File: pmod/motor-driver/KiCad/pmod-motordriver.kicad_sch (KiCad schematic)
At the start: 14 parts, among them J1 Conn_01x06_Pin, J2 Screw_Terminal_01x02, J3 Screw_Terminal_01x02, J4 Screw_Terminal_01x02, Q1 AO3401A, U1 DRV8833PWP

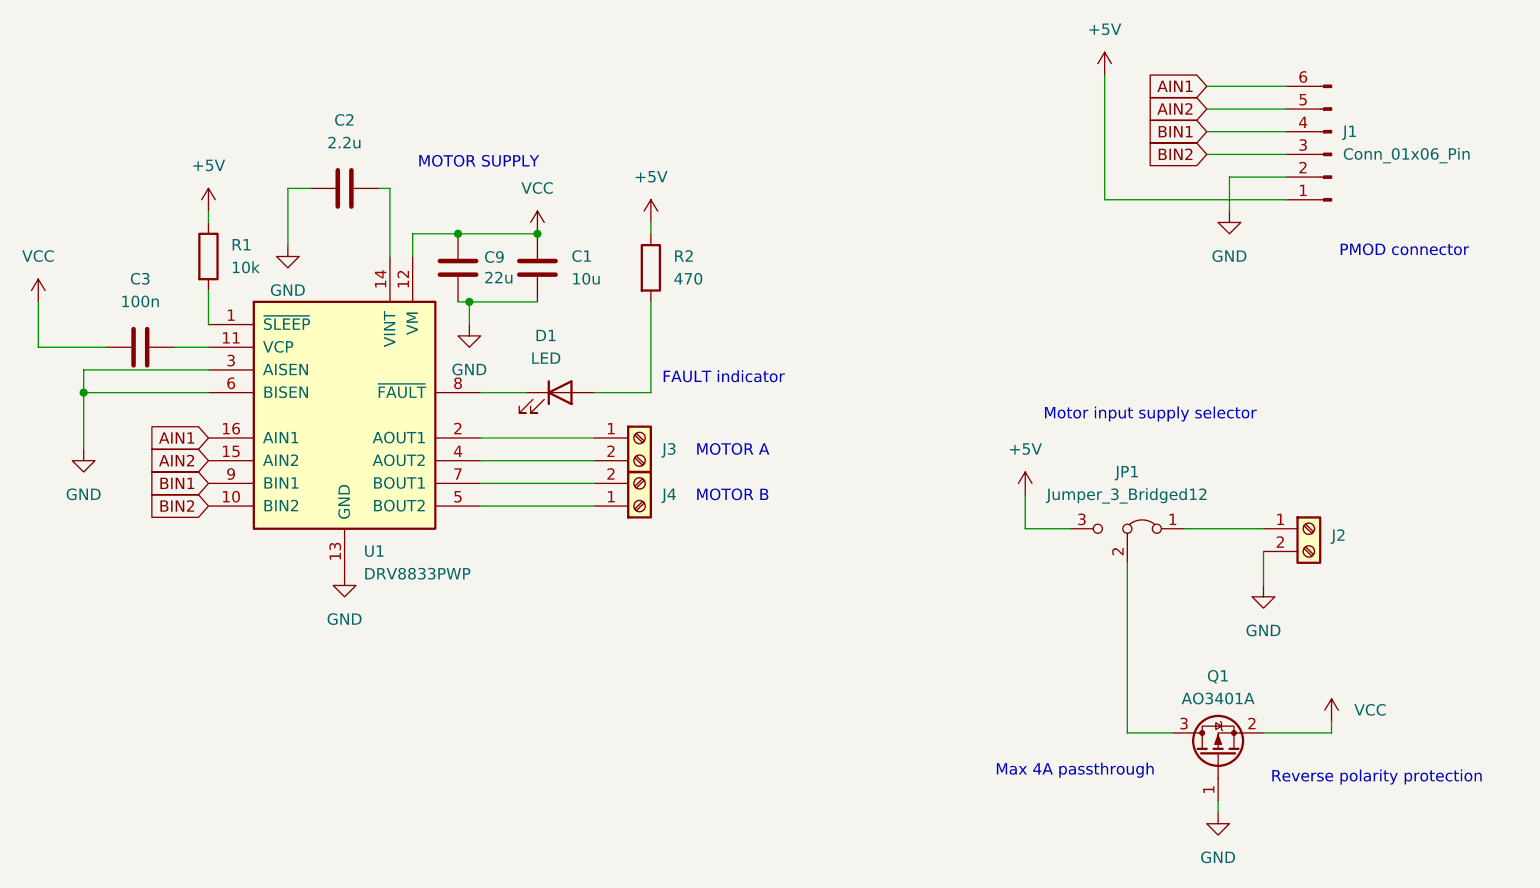
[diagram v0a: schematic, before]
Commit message: update motor driver
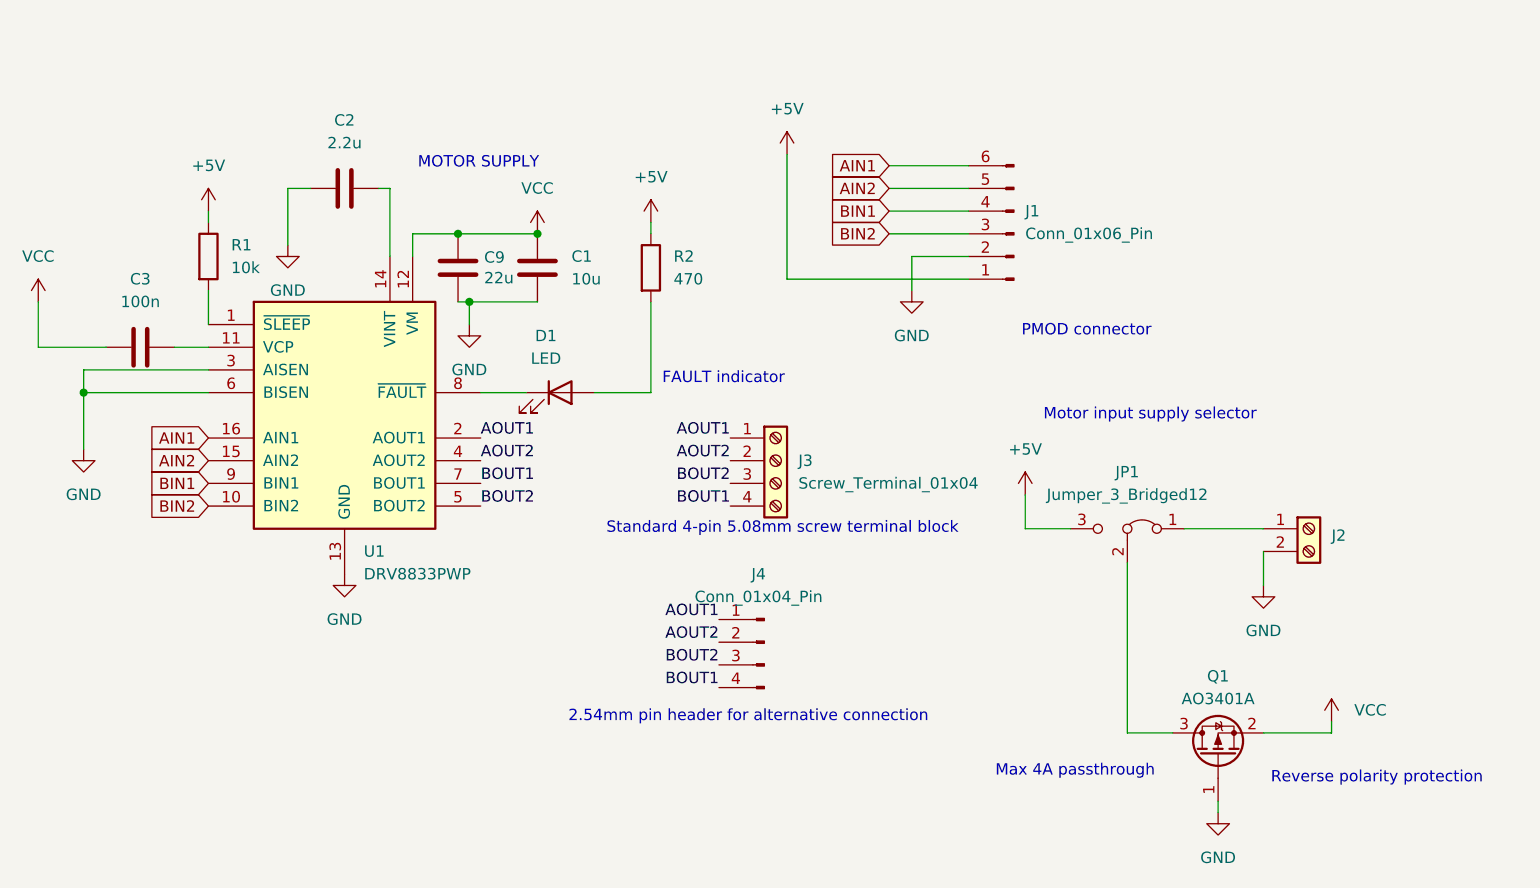
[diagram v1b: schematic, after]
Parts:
- removed J3, J4: Screw_Terminal_01x02, TerminalBlock_TE-Connectivity:TerminalBlock_TE_282834-2_1x02_P2.54mm_Horizontal, symbol Connector:Screw_Terminal_01x02
- added J3: Screw_Terminal_01x04, TerminalBlock:TerminalBlock_bornier-4_P5.08mm, symbol Connector:Screw_Terminal_01x04
- added J4: Conn_01x04_Pin, Connector_PinHeader_2.54mm:PinHeader_1x04_P2.54mm_Vertical, symbol Connector:Conn_01x04_Pin
- J2: footprint TerminalBlock_TE-Connectivity:TerminalBlock_TE_282834-2_1x02_P2.54mm_Horizontal -> TerminalBlock:TerminalBlock_bornier-2_P5.08mm
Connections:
- net BOUT2: now reaches U1.5 (BOUT2)
- net BOUT2: now also J3.3 (Pin_3), J4.3 (Pin_3)
- net BOUT1: now reaches U1.7 (BOUT1)
- net BOUT1: now also J3.4 (Pin_4), J4.4 (Pin_4)
- net AOUT1: now reaches U1.2 (AOUT1)
- net AOUT1: now also J3.1 (Pin_1), J4.1 (Pin_1)
- net AOUT2: now reaches U1.4 (AOUT2)
- net AOUT2: now also J3.2 (Pin_2), J4.2 (Pin_2)
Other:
- note added: "2.54mm pin header for alternative connection"
- note added: "Standard 4-pin 5.08mm screw terminal block"
- note removed: "MOTOR A"
- note removed: "MOTOR B"
- moved on the sheet: J1

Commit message: add missing id to motor driver
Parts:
- J3: LCSC (none) -> C2827883
- J4: LCSC (none) -> C124378
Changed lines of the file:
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@@
+			)
+		)
+		(property "LCSC" "C124378"
+			(at 147.32 121.92 0)
+			(effects
+				(font
+					(size 1.27 1.27)
+				)
+				(hide yes)
 			)
 		)
@@
 			(at 148.59 101.6 0)
 			(effects
+				(font
+					(size 1.27 1.27)
+				)
+				(hide yes)
+			)
+		)
+		(property "LCSC" "C2827883"
+			(at 148.59 101.6 0)
+			(effects

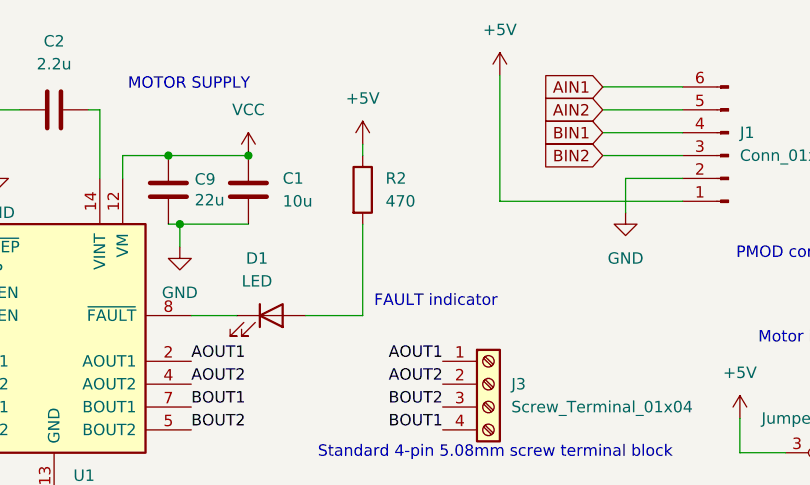
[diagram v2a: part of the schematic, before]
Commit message: replace LED resistor in motor-driver
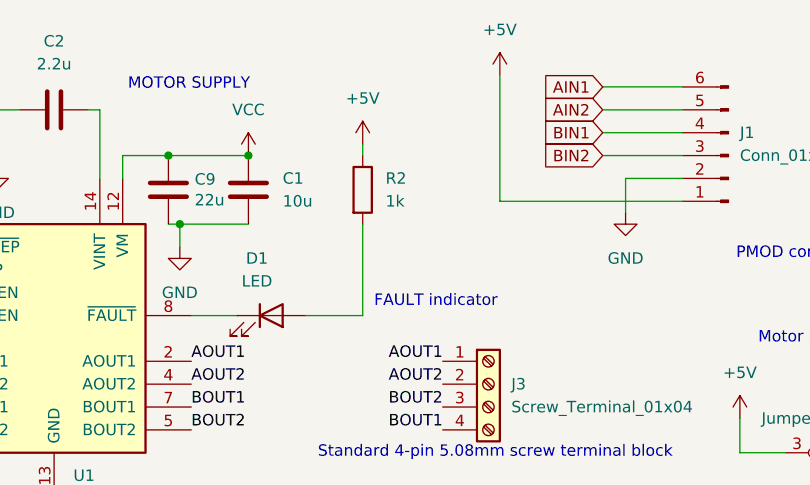
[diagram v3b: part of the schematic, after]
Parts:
- R2: value 470 -> 1k; LCSC C23179 -> C21190
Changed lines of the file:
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@@
 			)
 		)
-		(property "Value" "470"
+		(property "Value" "1k"
 			(at 137.16 81.2799 0)
 			(effects
@@
 			)
 		)
-		(property "LCSC" "C23179"
+		(property "LCSC" "C21190"
 			(at 134.62 80.01 0)
 			(effects
